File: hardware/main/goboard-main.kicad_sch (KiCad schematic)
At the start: 0 parts

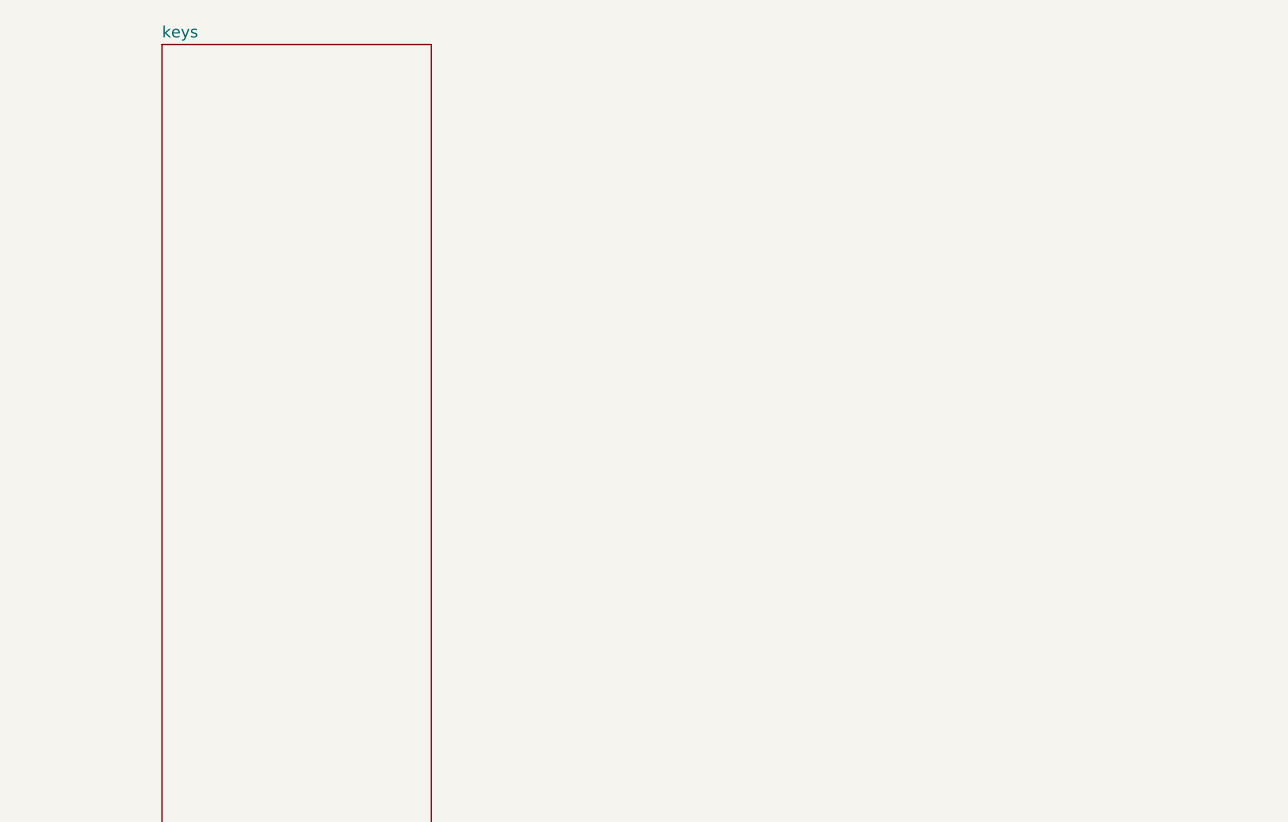
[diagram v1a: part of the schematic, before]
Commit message: Add circuit for the shift registers
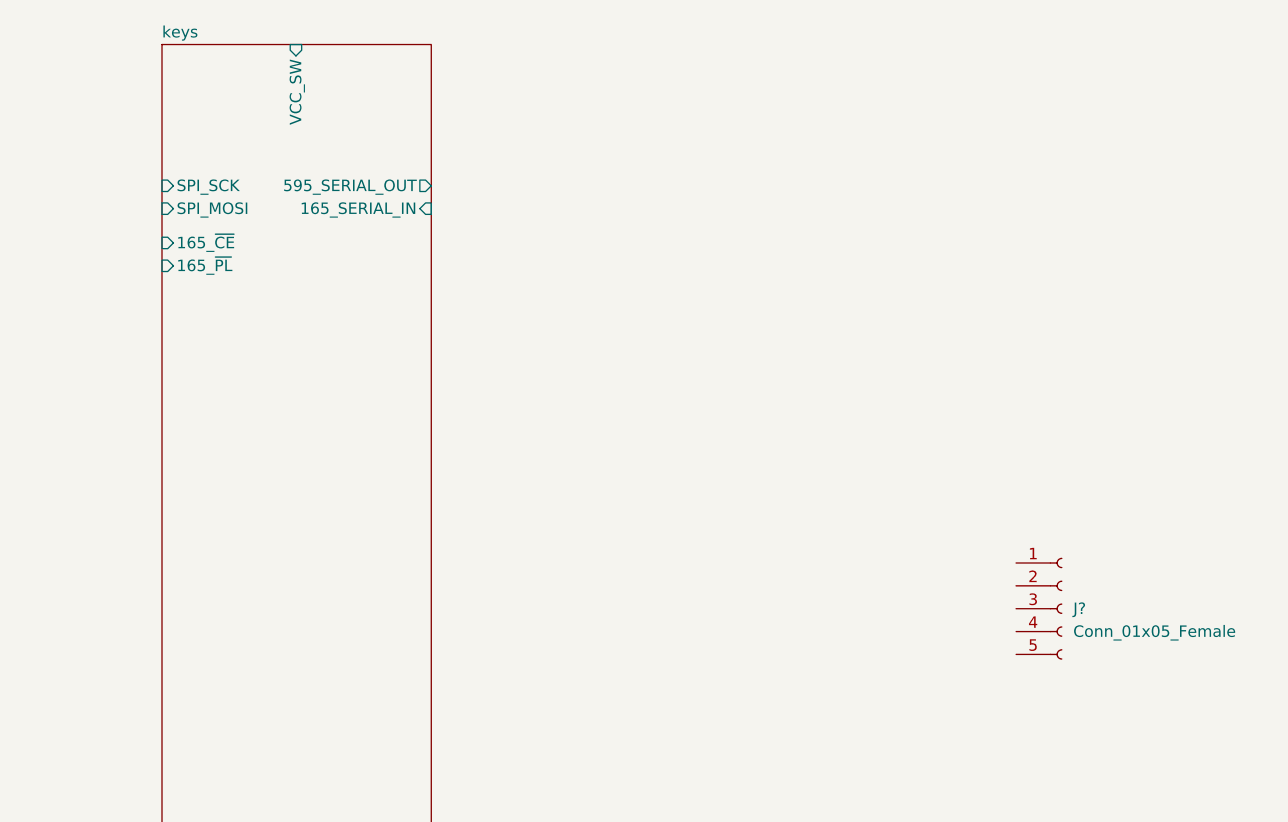
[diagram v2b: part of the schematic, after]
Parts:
- added J?: Conn_01x05_Female, symbol Connector:Conn_01x05_Female
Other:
- sheet keys ports: added 165_SERIAL_IN, 165_~CE, 165_~PL, 595_SERIAL_OUT, SPI_MOSI, SPI_SCK, VCC_SW; removed none
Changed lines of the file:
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@@
 (kicad_sch (version 20201015) (generator eeschema)
   (paper "A4")
+  (symbol (lib_id "Connector:Conn_01x05_Female") (at 261.62 101.6 0) (unit 1)
+    (in_bom yes) (on_board yes)
+    (property "Reference" "J?" (id 0) (at 262.89 101.6 0)
+      (effects (font (size 1.27 1.27)) (justify left))
+    )
+    (property "Value" "Conn_01x05_Female" (id 1) (at 262.89 104.14 0)
+      (effects (font (size 1.27 1.27)) (justify left))
+    )
+    (property "Footprint" "" (id 2) (at 261.62 101.6 0)
+      (effects (font (size 1.27 1.27)) hide)
+    )
+    (property "Datasheet" "~" (id 3) (at 261.62 101.6 0)
+      (effects (font (size 1.27 1.27)) hide)
+    )
+  )
   (sheet (at 100.1268 38.6588) (size 40.8432 115.0112)
     (stroke (width 0.001) (type solid) (color 132 0 132 1))
@@
     (property "Dateiname Blatt" "keys.kicad_sch" (id 1) (at 161.6456 147.6765 0)
       (effects (font (size 1.27 1.27)) (justify left top))
+    )
+    (pin "VCC_SW" input (at 176.53 38.9128 90)
+      (effects (font (size 1.27 1.27)) (justify right))
+    )
+    (pin "SPI_SCK" input (at 161.6456 54.61 180)
+      (effects (font (size 1.27 1.27)) (justify left))
+    )
+    (pin "SPI_MOSI" input (at 161.6456 57.15 180)
+      (effects (font (size 1.27 1.27)) (justify left))
+    )
+    (pin "165_~CE" input (at 161.6456 60.96 180)
+      (effects (font (size 1.27 1.27)) (justify left))
+    )
+    (pin "165_~PL" input (at 161.6456 63.5 180)
+      (effects (font (size 1.27 1.27)) (justify left))
+    )
+    (pin "595_SERIAL_OUT" output (at 191.5668 54.61 0)
+      (effects (font (size 1.27 1.27)) (justify right))
+    )
+    (pin "165_SERIAL_IN" input (at 191.5668 57.15 0)
+      (effects (font (size 1.27 1.27)) (justify right))
     )
   )
@@
   )
   (symbol_instances
+    (path "/791bf4bc-b52e-43a7-af69-54454aa52998"
+      (reference "J?") (unit 1) (value "Conn_01x05_Female") (footprint "")
+    )
+    (path "/d1d7b976-c206-4a6a-bf43-9e0a3d3fc0a5/28c8ce99-9074-40f3-bd9b-48b6c7957fa0"
+      (reference "D?") (unit 1) (value "Scroll Lock") (footprint "")
+    )
+    (path "/d1d7b976-c206-4a6a-bf43-9e0a3d3fc0a5/65ad0a10-5aa4-47d9-be7a-0521ecdabe84"
+      (reference "D?") (unit 1) (value "Power") (footprint "")
+    )
+    (path "/d1d7b976-c206-4a6a-bf43-9e0a3d3fc0a5/f67dadd6-dad2-4607-839c-e26e0dbb5444"
+      (reference "D?") (unit 1) (value "Caps Lock") (footprint "")
+    )
+    (path "/d1d7b976-c206-4a6a-bf43-9e0a3d3fc0a5/ce8d2f41-d04c-40e3-bb10-8d13b7a0504a"
+      (reference "U4") (unit 1) (value "Holyiot-18010-NRF52840") (footprint "footprints:Holyiot-18010-NRF52840")
+    )
+    (path "/6ef23857-23de-44e2-ab0d-92ef0bfe30b4/415e5a81-d53b-4540-bd26-214578d9701e"
+      (reference "#PWR?") (unit 1) (value "GND") (footprint "")
+    )
+    (path "/6ef23857-23de-44e2-ab0d-92ef0bfe30b4/d1e9850a-ee04-45d7-a3f4-2f8d46f4d83e"
+      (reference "#PWR?") (unit 1) (value "GND") (footprint "")
+    )
+    (path "/6ef23857-23de-44e2-ab0d-92ef0bfe30b4/ea6a0ac9-9fb1-4de9-a96b-de03f212916c"
+      (reference "#PWR?") (unit 1) (value "GND") (footprint "")
+    )
+    (path "/6ef23857-23de-44e2-ab0d-92ef0bfe30b4/eed92e48-427b-49a9-b5d5-e33ccaca4eac"
+      (reference "#PWR?") (unit 1) (value "GND") (footprint "")
+    )
+    (path "/6ef23857-23de-44e2-ab0d-92ef0bfe30b4/6a93893d-c57b-4ddc-bb76-9b4cd649dbbf"
+      (reference "C?") (unit 1) (value "100nF") (footprint "")
+    )
+    (path "/6ef23857-23de-44e2-ab0d-92ef0bfe30b4/ddaf9607-7357-4202-8c81-9e30a6b78ba4"
+      (reference "C?") (unit 1) (value "100nF") (footprint "")
+    )
+    (path "/6ef23857-23de-44e2-ab0d-92ef0bfe30b4/ec74ff31-b340-489c-a0ef-465d7e0a1e59"
+      (reference "C?") (unit 1) (value "100nF") (footprint "")
+    )
     (path "/6ef23857-23de-44e2-ab0d-92ef0bfe30b4/187e24d7-87a7-452e-afe1-e0a94b806893"
       (reference "D1") (unit 1) (value "BAT54C") (footprint "Package_TO_SOT_SMD:SOT-23")
@@
       (reference "SW87") (unit 1) (value "x") (footprint "footprints:SW_Cherry_MX_1.00u_PCB")
     )
-    (path "/6ef23857-23de-44e2-ab0d-92ef0bfe30b4/96c47e32-5b4a-4e9f-b841-a14a1bfd0d4c"
-      (reference "U1") (unit 1) (value "74LV595") (footprint "Package_SO:TSSOP-16_4.4x5mm_P0.65mm")
-    )
-    (path "/6ef23857-23de-44e2-ab0d-92ef0bfe30b4/baef4c0e-08b8-4895-9c18-753f10810b9a"
-      (reference "U2") (unit 1) (value "74LV165") (footprint "Package_SO:TSSOP-16_4.4x5mm_P0.65mm")
-    )
-    (path "/6ef23857-23de-44e2-ab0d-92ef0bfe30b4/5f52de7c-4ac1-4261-a687-65bf4c626c2a"
-      (reference "U3") (unit 1) (value "74LV165") (footprint "Package_SO:TSSOP-16_4.4x5mm_P0.65mm")
+    (path "/6ef23857-23de-44e2-ab0d-92ef0bfe30b4/5171c6b2-dca1-48dd-b43f-d303f7ee6e30"
+      (reference "U?") (unit 1) (value "74LV165") (footprint "Package_SO:TSSOP-16_4.4x5mm_P0.65mm")
+    )
+    (path "/6ef23857-23de-44e2-ab0d-92ef0bfe30b4/71c255af-3715-4d11-87c9-9df79aa675c7"
+      (reference "U?") (unit 1) (value "74LV595") (footprint "Package_SO:TSSOP-16_4.4x5mm_P0.65mm")
+    )
+    (path "/6ef23857-23de-44e2-ab0d-92ef0bfe30b4/bd1ecbe1-4f71-49c2-aa4c-b2e67c4ed577"
+      (reference "U?") (unit 1) (value "74LV165") (footprint "Package_SO:TSSOP-16_4.4x5mm_P0.65mm")
     )
   )

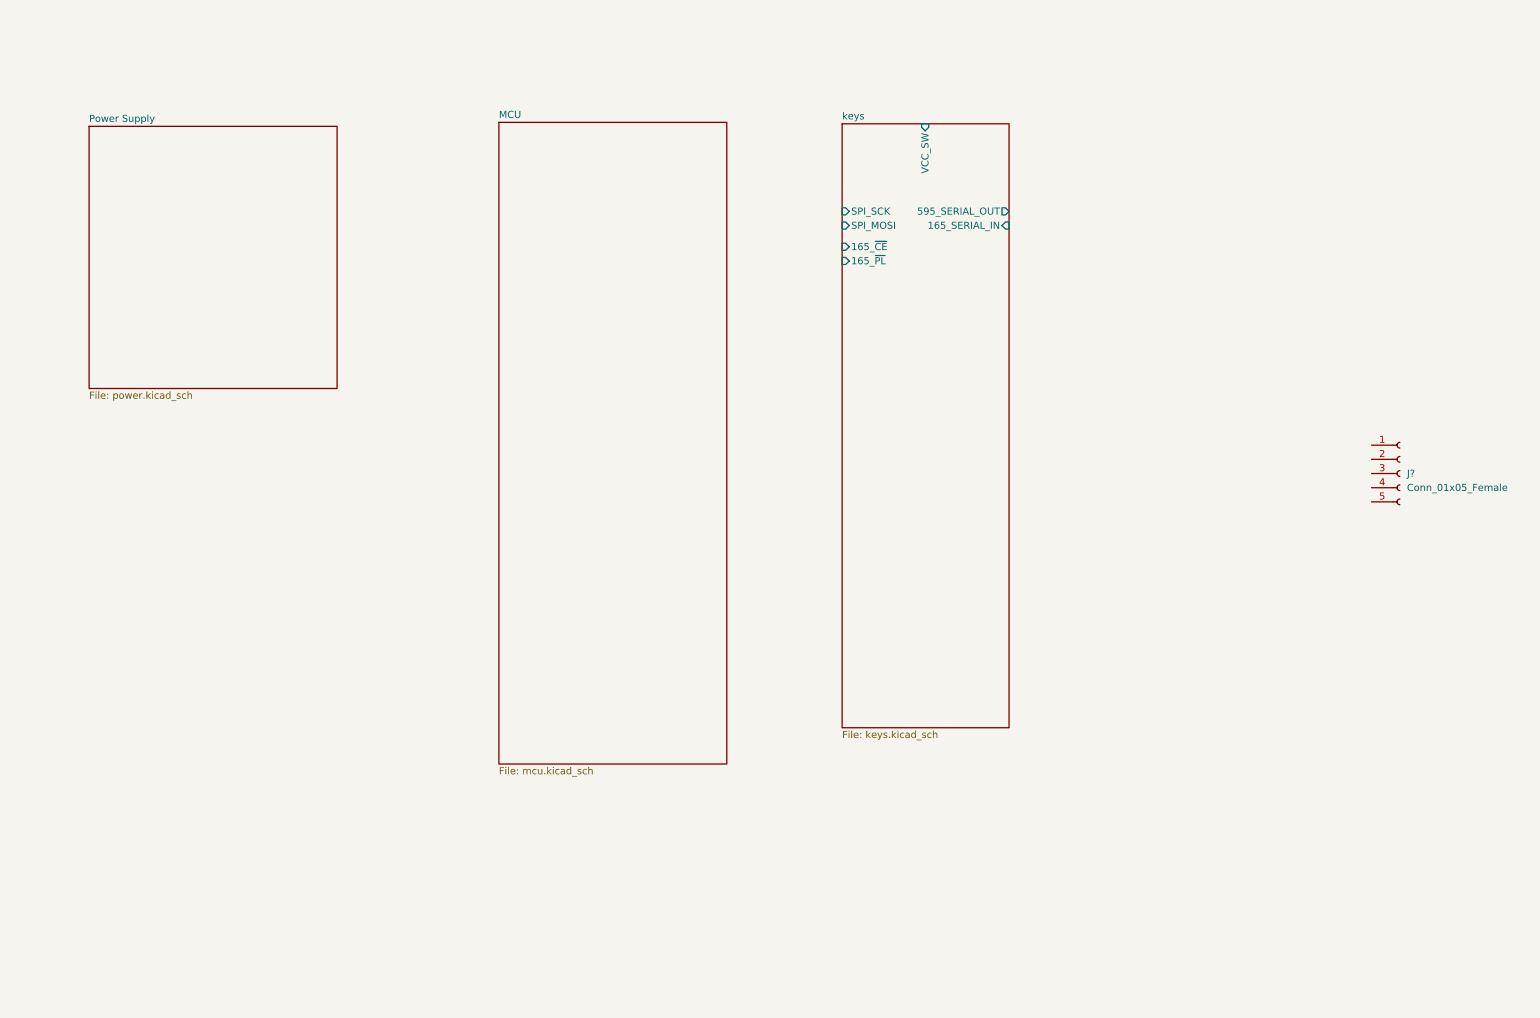
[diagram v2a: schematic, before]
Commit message: Add circuit for the USB-connector
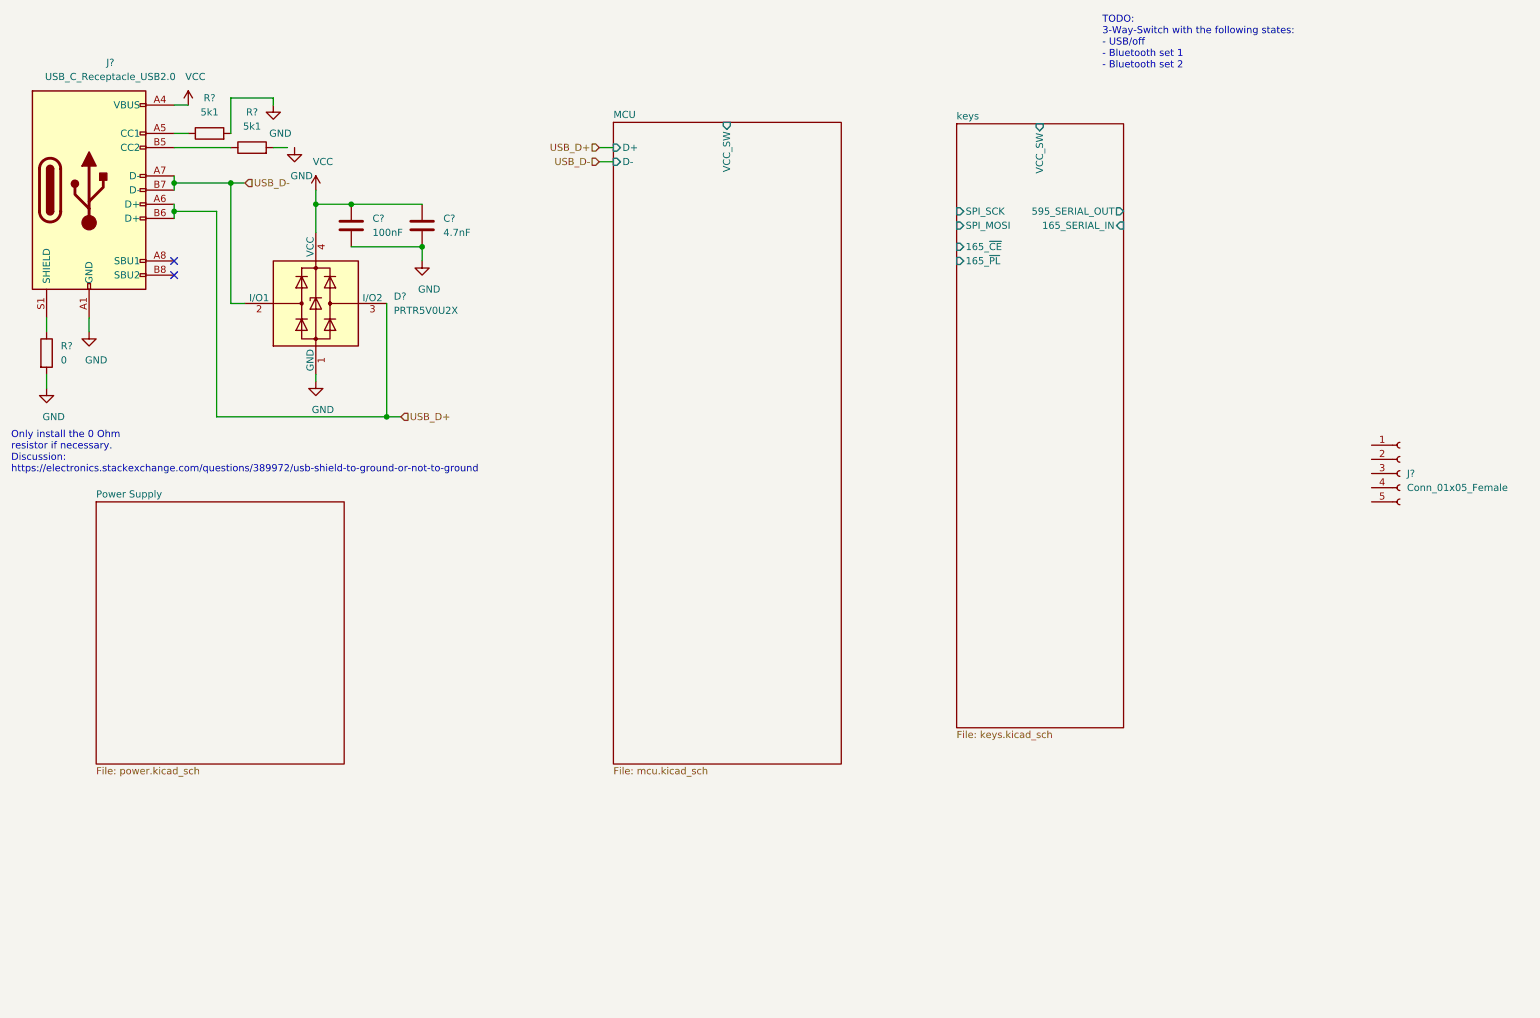
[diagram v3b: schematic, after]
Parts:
- added C?: 4.7nF, symbol Device:C
- added C?: 100nF, symbol Device:C
- added D?: PRTR5V0U2X, Package_TO_SOT_SMD:SOT-143, symbol Power_Protection:PRTR5V0U2X
- added J?: USB_C_Receptacle_USB2.0, footprints:USB_C_Receptale_JAE_DX07S016JA1R1500, symbol Connector:USB_C_Receptacle_USB2.0
- added R? (x2): 5k1, symbol Device:R
- added R?: 0, symbol Device:R
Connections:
- new net: J?.B5 (CC2), R?.1
- new net: J?.S1 (SHIELD), R?.1
- new net: J?.A5 (CC1), R?.1
- new net GND: C?.2, C?.2, D?.1 (GND), J?.A1 (GND), J?.A12 (GND), J?.B1 (GND), J?.B12 (GND), R?.2, R?.2
- new net USB_D+: D?.3 (I/O2), J?.A6 (D+), J?.B6 (D+)
- new net USB_D-: D?.2 (I/O1), J?.A7 (D-), J?.B7 (D-)
- new net VCC: C?.1, C?.1, D?.4 (VCC), J?.A4 (VBUS), J?.A9 (VBUS), J?.B4 (VBUS), J?.B9 (VBUS)
- no-connect marks 0 -> 2
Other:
- sheet MCU ports: added D+, D-, VCC_SW; removed none
- note added: "Only install the 0 Ohm resistor if necessary. Discussion: https://electronics.stackexchange.com/questions/389972/usb-shield-to-ground-or-not-to-ground"
- note added: "TODO: 3-Way-Switch with the following states: - USB/off - Bluetooth set 1 - Bluetooth set 2"

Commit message: Update the PCB
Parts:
- gave numbers to parts that had none: 8
